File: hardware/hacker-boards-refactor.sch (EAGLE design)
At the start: 38 parts, among them J1 MICRO_USB_B_JST_MC5BR3-M404-4S

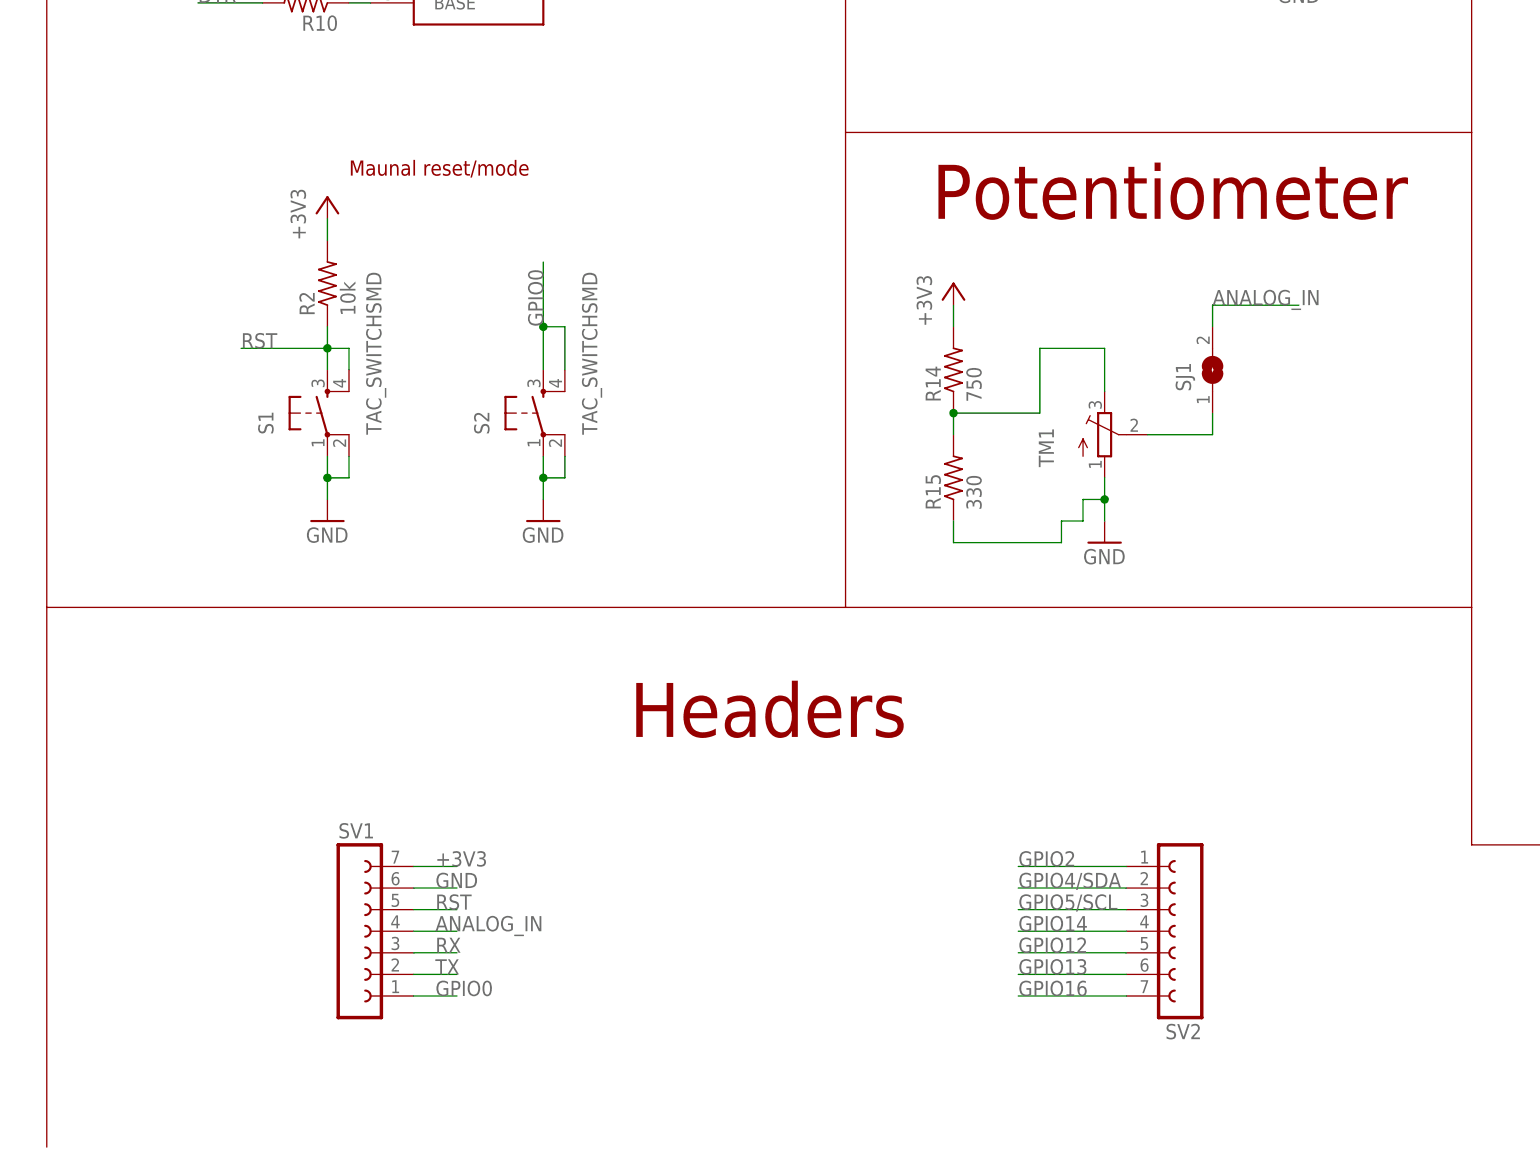
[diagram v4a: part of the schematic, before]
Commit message: Slightly enlarged board for new headers, extensively tweaked silkscreen
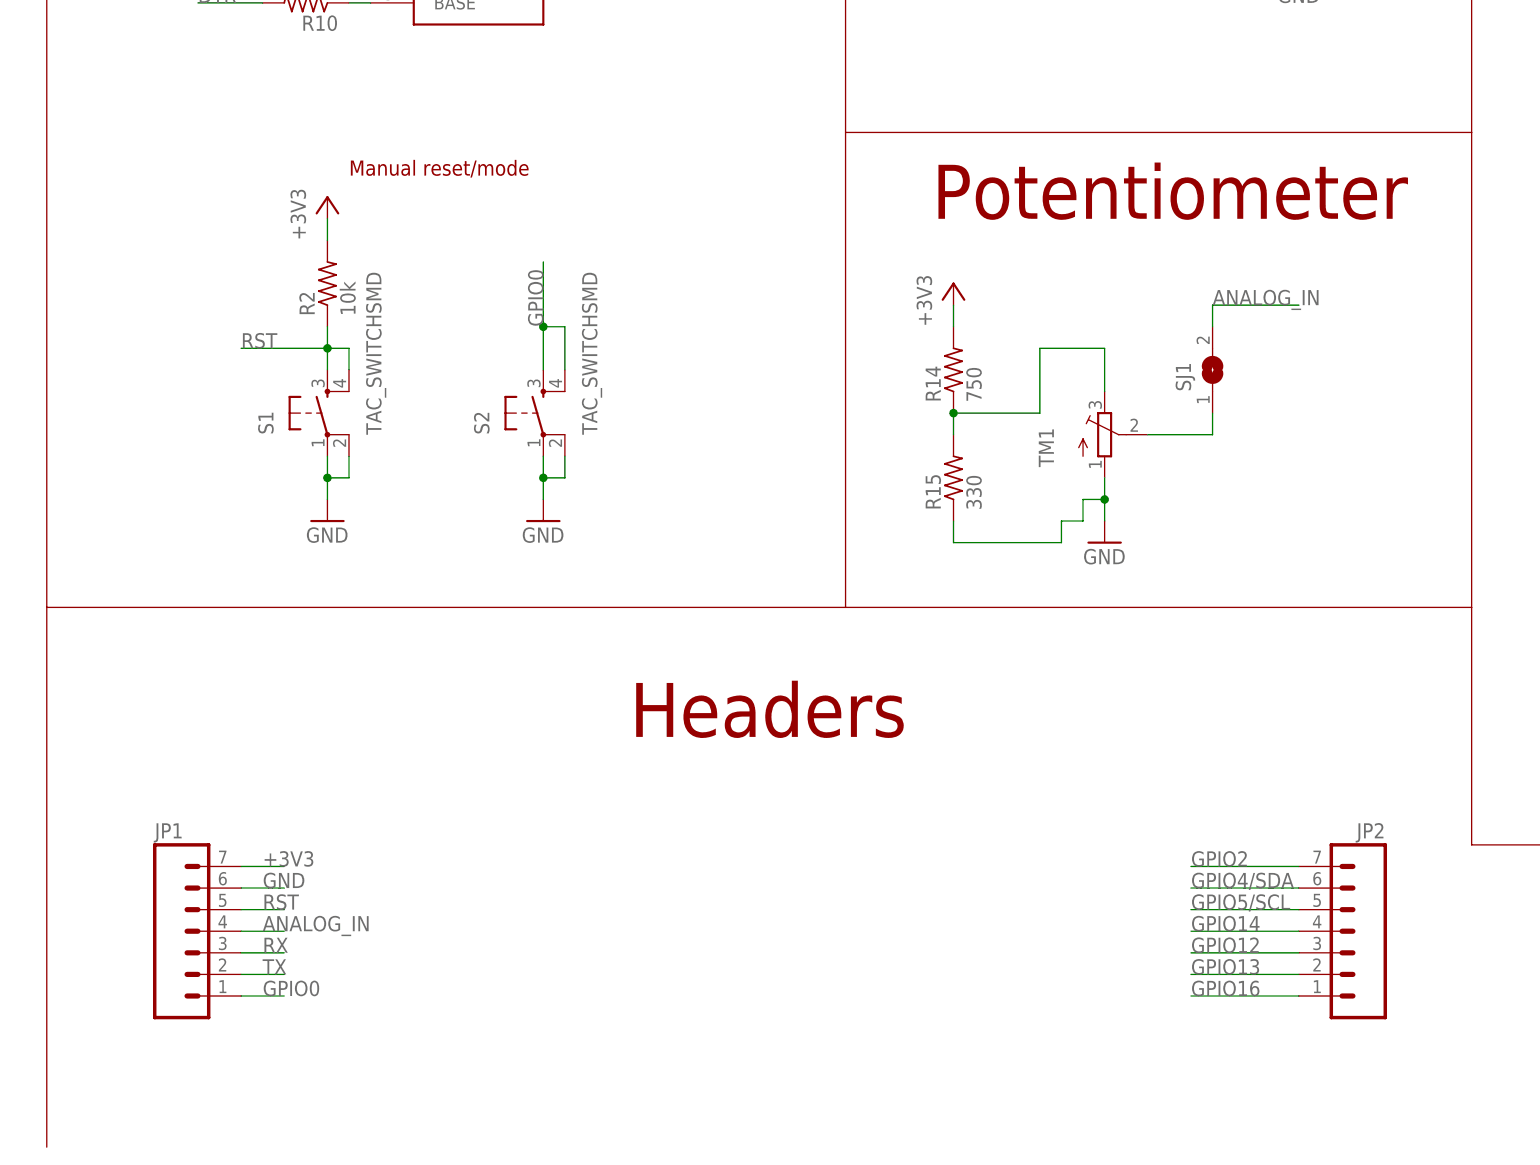
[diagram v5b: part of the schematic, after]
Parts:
- removed SV1, SV2: (no value), con-lsta:FE07-1
- added JP1, JP2: (no value), hacker-board:M07LONGPADS
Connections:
- net +3V3: now also JP1.7; no longer SV1.7
- net ANALOG_IN: now also JP1.4; no longer SV1.4
- net GND: now also JP1.6; no longer SV1.6
- net GPIO0: now also JP1.1; no longer SV1.1
- net GPIO12: now also JP2.3; no longer SV2.5
- net GPIO13: now also JP2.2; no longer SV2.6
- net GPIO14: now also JP2.4; no longer SV2.4
- net GPIO16: now also JP2.1; no longer SV2.7
- net GPIO2: now also JP2.7; no longer SV2.1
- net GPIO4/SDA: now also JP2.6; no longer SV2.2
- net GPIO5/SCL: now also JP2.5; no longer SV2.3
- net RST: now also JP1.5; no longer SV1.5
- net RX: now also JP1.3; no longer SV1.3
- net TX: now also JP1.2; no longer SV1.2
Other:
- note added: "Manual reset/mode"
- note removed: "Maunal reset/mode"
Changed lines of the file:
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@@
 <?xml version="1.0" encoding="utf-8"?>
 <!DOCTYPE eagle SYSTEM "eagle.dtd">
-<eagle version="7.5.0">
+<eagle version="7.3.0">
 <drawing>
 <settings>
@@
 <part name="R9" library="resistor" deviceset="R-US_" device="R0805" value="10k"/>
 <part name="R10" library="resistor" deviceset="R-US_" device="R0805" value="10k"/>
-<part name="SV1" library="con-lsta" deviceset="FE07-1" device=""/>
 <part name="FRAME1" library="frames" deviceset="DINA3_L" device=""/>
-<part name="SV2" library="con-lsta" deviceset="FE07-1" device=""/>
 <part name="R11" library="resistor" deviceset="R-US_" device="R0805" value="330"/>
 <part name="C6" library="hacker-board" deviceset="C" device="0805" value="1uF"/>
@@
 <part name="P+3" library="supply1" deviceset="+5V" device=""/>
 <part name="U$3" library="hacker-board" deviceset="CP2104" device=""/>
+<part name="JP1" library="hacker-board" deviceset="M07" device="LONGPADS"/>
+<part name="JP2" library="hacker-board" deviceset="M07" device="LONGPADS"/>
 </parts>
 <sheets>
@@
 <text x="124.46" y="91.44" size="1.778" layer="94">Pull-up/pull-down resistors</text>
 <text x="33.02" y="71.12" size="1.778" layer="94">Reset/bootloader mode from USB/UART chip</text>
-<text x="43.18" y="22.86" size="1.778" layer="94">Maunal reset/mode</text>
+<text x="43.18" y="22.86" size="1.778" layer="94">Manual reset/mode</text>
 <text x="210.82" y="60.96" size="1.778" layer="94">Power LED</text>
 <text x="256.54" y="60.96" size="1.778" layer="94">Mode LED</text>
@@
 <instance part="R9" gate="G$1" x="38.1" y="60.96" rot="R180"/>
 <instance part="R10" gate="G$1" x="38.1" y="43.18" rot="R180"/>
-<instance part="SV1" gate="G$1" x="43.18" y="-66.04"/>
 <instance part="FRAME1" gate="G$1" x="-93.98" y="-91.44"/>
 <instance part="FRAME1" gate="G$2" x="193.04" y="-91.44"/>
-<instance part="SV2" gate="G$1" x="142.24" y="-66.04" rot="R180"/>
 <instance part="R11" gate="G$1" x="200.66" y="-22.86" rot="R180"/>
 <instance part="C6" gate="G$1" x="236.22" y="-7.62"/>
@@
 <instance part="P+3" gate="1" x="-78.74" y="-27.94" rot="R90"/>
 <instance part="U$3" gate="G$1" x="-38.1" y="-30.48"/>
+<instance part="JP1" gate="G$1" x="25.4" y="-68.58"/>
+<instance part="JP2" gate="G$1" x="160.02" y="-68.58" rot="MR0"/>
 </instances>
 <busses>
@@
 </segment>
 <segment>
-<pinref part="SV1" gate="G$1" pin="7"/>
-<wire x1="50.8" y1="-58.42" x2="55.88" y2="-58.42" width="0.1524" layer="91"/>
-<label x="53.34" y="-58.42" size="1.778" layer="95"/>
-</segment>
-<segment>
 <pinref part="+3V11" gate="G$1" pin="+3V3"/>
 <pinref part="R14" gate="G$1" pin="2"/>
 <wire x1="114.3" y1="7.62" x2="114.3" y2="5.08" width="0.1524" layer="91"/>
+</segment>
+<segment>
+<pinref part="JP1" gate="G$1" pin="7"/>
+<wire x1="30.48" y1="-58.42" x2="35.56" y2="-58.42" width="0.1524" layer="91"/>
+<label x="33.02" y="-58.42" size="1.778" layer="95"/>
 </segment>
 </net>
@@
 <wire x1="-5.08" y1="104.14" x2="-5.08" y2="99.06" width="0.1524" layer="91"/>
 <pinref part="GND10" gate="1" pin="GND"/>
-</segment>
-<segment>
-<pinref part="SV1" gate="G$1" pin="6"/>
-<wire x1="50.8" y1="-60.96" x2="55.88" y2="-60.96" width="0.1524" layer="91"/>
-<label x="53.34" y="-60.96" size="1.778" layer="95"/>
 </segment>
 <segment>
@@
 <junction x="132.08" y="-15.24"/>
 </segment>
+<segment>
+<pinref part="JP1" gate="G$1" pin="6"/>
+<wire x1="30.48" y1="-60.96" x2="35.56" y2="-60.96" width="0.1524" layer="91"/>
+<label x="33.02" y="-60.96" size="1.778" layer="95"/>
+</segment>
 </net>
 <net name="RST" class="0">
@@
 </segment>
 <segment>
-<pinref part="SV1" gate="G$1" pin="5"/>
-<wire x1="50.8" y1="-63.5" x2="55.88" y2="-63.5" width="0.1524" layer="91"/>
-<label x="53.34" y="-63.5" size="1.778" layer="95"/>
+<pinref part="JP1" gate="G$1" pin="5"/>
+<wire x1="30.48" y1="-63.5" x2="35.56" y2="-63.5" width="0.1524" layer="91"/>
+<label x="33.02" y="-63.5" size="1.778" layer="95"/>
 </segment>
 </net>
@@
 <wire x1="71.12" y1="132.08" x2="58.42" y2="132.08" width="0.1524" layer="91"/>
 <label x="58.42" y="132.08" size="1.778" layer="95"/>
-</segment>
-<segment>
-<pinref part="SV1" gate="G$1" pin="4"/>
-<wire x1="50.8" y1="-66.04" x2="55.88" y2="-66.04" width="0.1524" layer="91"/>
-<label x="53.34" y="-66.04" size="1.778" layer="95"/>
 </segment>
 <segment>
@@
 <label x="144.78" y="7.62" size="1.778" layer="95"/>
 </segment>
+<segment>
+<pinref part="JP1" gate="G$1" pin="4"/>
+<wire x1="30.48" y1="-66.04" x2="35.56" y2="-66.04" width="0.1524" layer="91"/>
+<label x="33.02" y="-66.04" size="1.778" layer="95"/>
+</segment>
 </net>
 <net name="GPIO14" class="0">
@@
 </segment>
 <segment>
-<pinref part="SV2" gate="G$1" pin="4"/>
-<wire x1="134.62" y1="-66.04" x2="121.92" y2="-66.04" width="0.1524" layer="91"/>
-<label x="121.92" y="-66.04" size="1.778" layer="95"/>
+<pinref part="JP2" gate="G$1" pin="4"/>
+<wire x1="154.94" y1="-66.04" x2="142.24" y2="-66.04" width="0.1524" layer="91"/>
+<label x="142.24" y="-66.04" size="1.778" layer="95"/>
 </segment>
 </net>
@@
 </segment>
 <segment>
-<pinref part="SV2" gate="G$1" pin="5"/>
-<wire x1="134.62" y1="-68.58" x2="121.92" y2="-68.58" width="0.1524" layer="91"/>
-<label x="121.92" y="-68.58" size="1.778" layer="95"/>
+<pinref part="JP2" gate="G$1" pin="3"/>
+<wire x1="154.94" y1="-68.58" x2="142.24" y2="-68.58" width="0.1524" layer="91"/>
+<label x="142.24" y="-68.58" size="1.778" layer="95"/>
 </segment>
 </net>
@@
 </segment>
 <segment>
-<pinref part="SV2" gate="G$1" pin="6"/>
-<wire x1="134.62" y1="-71.12" x2="121.92" y2="-71.12" width="0.1524" layer="91"/>
-<label x="121.92" y="-71.12" size="1.778" layer="95"/>
+<pinref part="JP2" gate="G$1" pin="2"/>
+<wire x1="154.94" y1="-71.12" x2="142.24" y2="-71.12" width="0.1524" layer="91"/>
+<label x="142.24" y="-71.12" size="1.778" layer="95"/>
 </segment>
 </net>
@@
 </segment>
 <segment>
-<pinref part="SV2" gate="G$1" pin="2"/>
-<wire x1="134.62" y1="-60.96" x2="121.92" y2="-60.96" width="0.1524" layer="91"/>
-<label x="121.92" y="-60.96" size="1.778" layer="95"/>
+<pinref part="JP2" gate="G$1" pin="6"/>
+<wire x1="154.94" y1="-60.96" x2="142.24" y2="-60.96" width="0.1524" layer="91"/>
+<label x="142.24" y="-60.96" size="1.778" layer="95"/>
 </segment>
 </net>
@@
 </segment>
 <segment>
-<pinref part="SV1" gate="G$1" pin="2"/>
-<wire x1="50.8" y1="-71.12" x2="55.88" y2="-71.12" width="0.1524" layer="91"/>
-<label x="53.34" y="-71.12" size="1.778" layer="95"/>
+<pinref part="JP1" gate="G$1" pin="2"/>
+<wire x1="30.48" y1="-71.12" x2="35.56" y2="-71.12" width="0.1524" layer="91"/>
+<label x="33.02" y="-71.12" size="1.778" layer="95"/>
 </segment>
 </net>
@@
 </segment>
 <segment>
-<pinref part="SV1" gate="G$1" pin="3"/>
-<wire x1="50.8" y1="-68.58" x2="55.88" y2="-68.58" width="0.1524" layer="91"/>
-<label x="53.34" y="-68.58" size="1.778" layer="95"/>
+<pinref part="JP1" gate="G$1" pin="3"/>
+<wire x1="30.48" y1="-68.58" x2="35.56" y2="-68.58" width="0.1524" layer="91"/>
+<label x="33.02" y="-68.58" size="1.778" layer="95"/>
 </segment>
 </net>
@@
 </segment>
 <segment>
-<pinref part="SV2" gate="G$1" pin="3"/>
-<wire x1="134.62" y1="-63.5" x2="121.92" y2="-63.5" width="0.1524" layer="91"/>
-<label x="121.92" y="-63.5" size="1.778" layer="95"/>
+<pinref part="JP2" gate="G$1" pin="5"/>
+<wire x1="154.94" y1="-63.5" x2="142.24" y2="-63.5" width="0.1524" layer="91"/>
+<label x="142.24" y="-63.5" size="1.778" layer="95"/>
 </segment>
 </net>
@@
 </segment>
 <segment>
-<pinref part="SV1" gate="G$1" pin="1"/>
-<wire x1="50.8" y1="-73.66" x2="55.88" y2="-73.66" width="0.1524" layer="91"/>
-<label x="53.34" y="-73.66" size="1.778" layer="95"/>
+<pinref part="JP1" gate="G$1" pin="1"/>
+<wire x1="30.48" y1="-73.66" x2="35.56" y2="-73.66" width="0.1524" layer="91"/>
+<label x="33.02" y="-73.66" size="1.778" layer="95"/>
 </segment>
 </net>
@@
 </segment>
 <segment>
-<pinref part="SV2" gate="G$1" pin="1"/>
-<wire x1="134.62" y1="-58.42" x2="121.92" y2="-58.42" width="0.1524" layer="91"/>
-<label x="121.92" y="-58.42" size="1.778" layer="95"/>
+<pinref part="JP2" gate="G$1" pin="7"/>
+<wire x1="154.94" y1="-58.42" x2="142.24" y2="-58.42" width="0.1524" layer="91"/>
+<label x="142.24" y="-58.42" size="1.778" layer="95"/>
 </segment>
 </net>
@@
 </segment>
 <segment>
-<pinref part="SV2" gate="G$1" pin="7"/>
-<wire x1="134.62" y1="-73.66" x2="121.92" y2="-73.66" width="0.1524" layer="91"/>
-<label x="121.92" y="-73.66" size="1.778" layer="95"/>
-</segment>
-<segment>
 <pinref part="R11" gate="G$1" pin="2"/>
 <wire x1="195.58" y1="-22.86" x2="187.96" y2="-22.86" width="0.1524" layer="91"/>
 <label x="187.96" y="-22.86" size="1.778" layer="95"/>
 </segment>
-</net>
+<segment>
+<pinref part="JP2" gate="G$1" pin="1"/>
+<wire x1="154.94" y1="-73.66" x2="142.24" y2="-73.66" width="0.1524" layer="91"/>
+<label x="142.24" y="-73.66" size="1.778" layer="95"/>
+</segment>
+</net>
